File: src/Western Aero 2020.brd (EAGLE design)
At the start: 127.7 x 101.9 mm, 94 parts, among them IC1 LT1963AET, IC2 LT1963AET, J1 PITOT, J10 ANA_IO, J11 PWR, J12 POWER, J2 BUZZER, J3 RX2/TX2, J4 RX3/TX3, J5 SPI, J6 DIG_IO, J7 RX1/TX1, J8 DIG_IO, J9 REF/GND, U3 TEENSY_3.5_DIL+4, U5 SPARKFUN_MPU9250_IMU, U6 ADAFRUIT_MPL3115A2_BAROMETER, U7 ADAFRUIT_INA219_BATTERY_SENSOR, U8 ADAFRUIT_RFM95W_LORA_RADIO, U9 ADAFRUIT_MTK3339_GPS

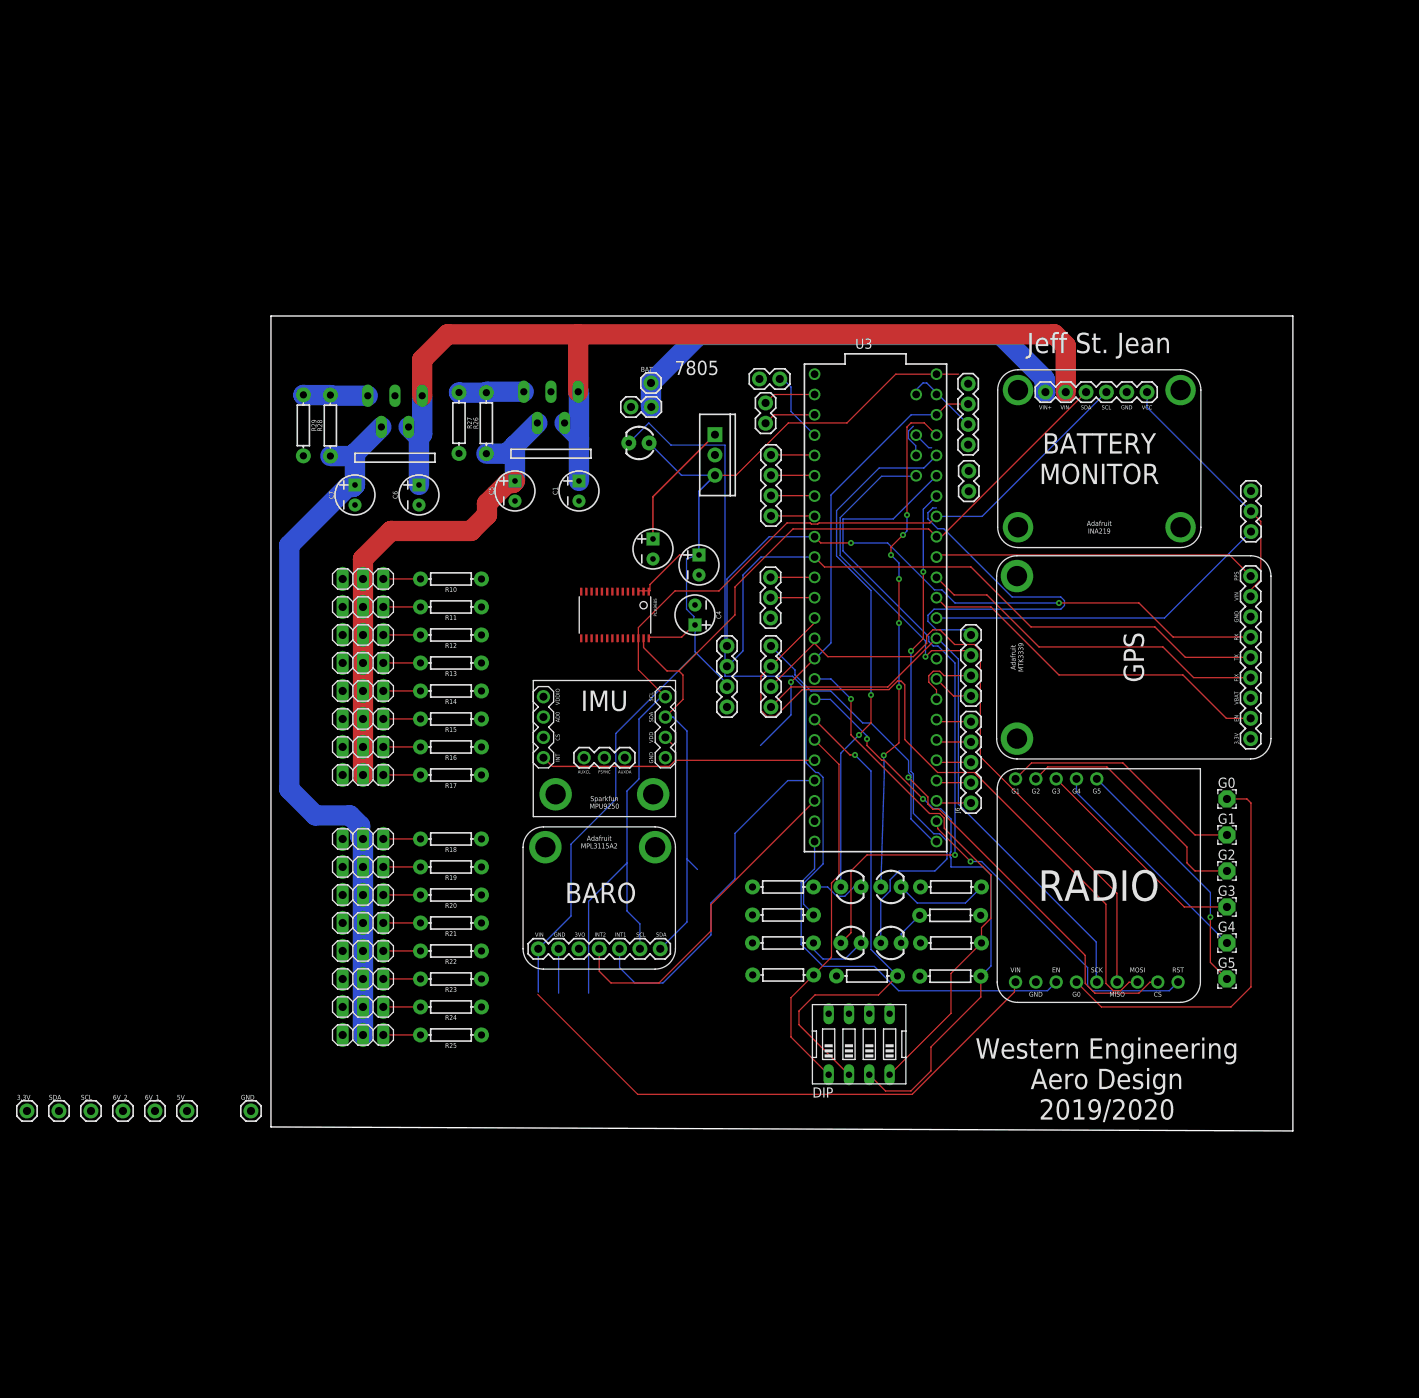
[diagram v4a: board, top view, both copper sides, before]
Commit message: Changed test point parts. Updated parts list. Adjusted board layout.
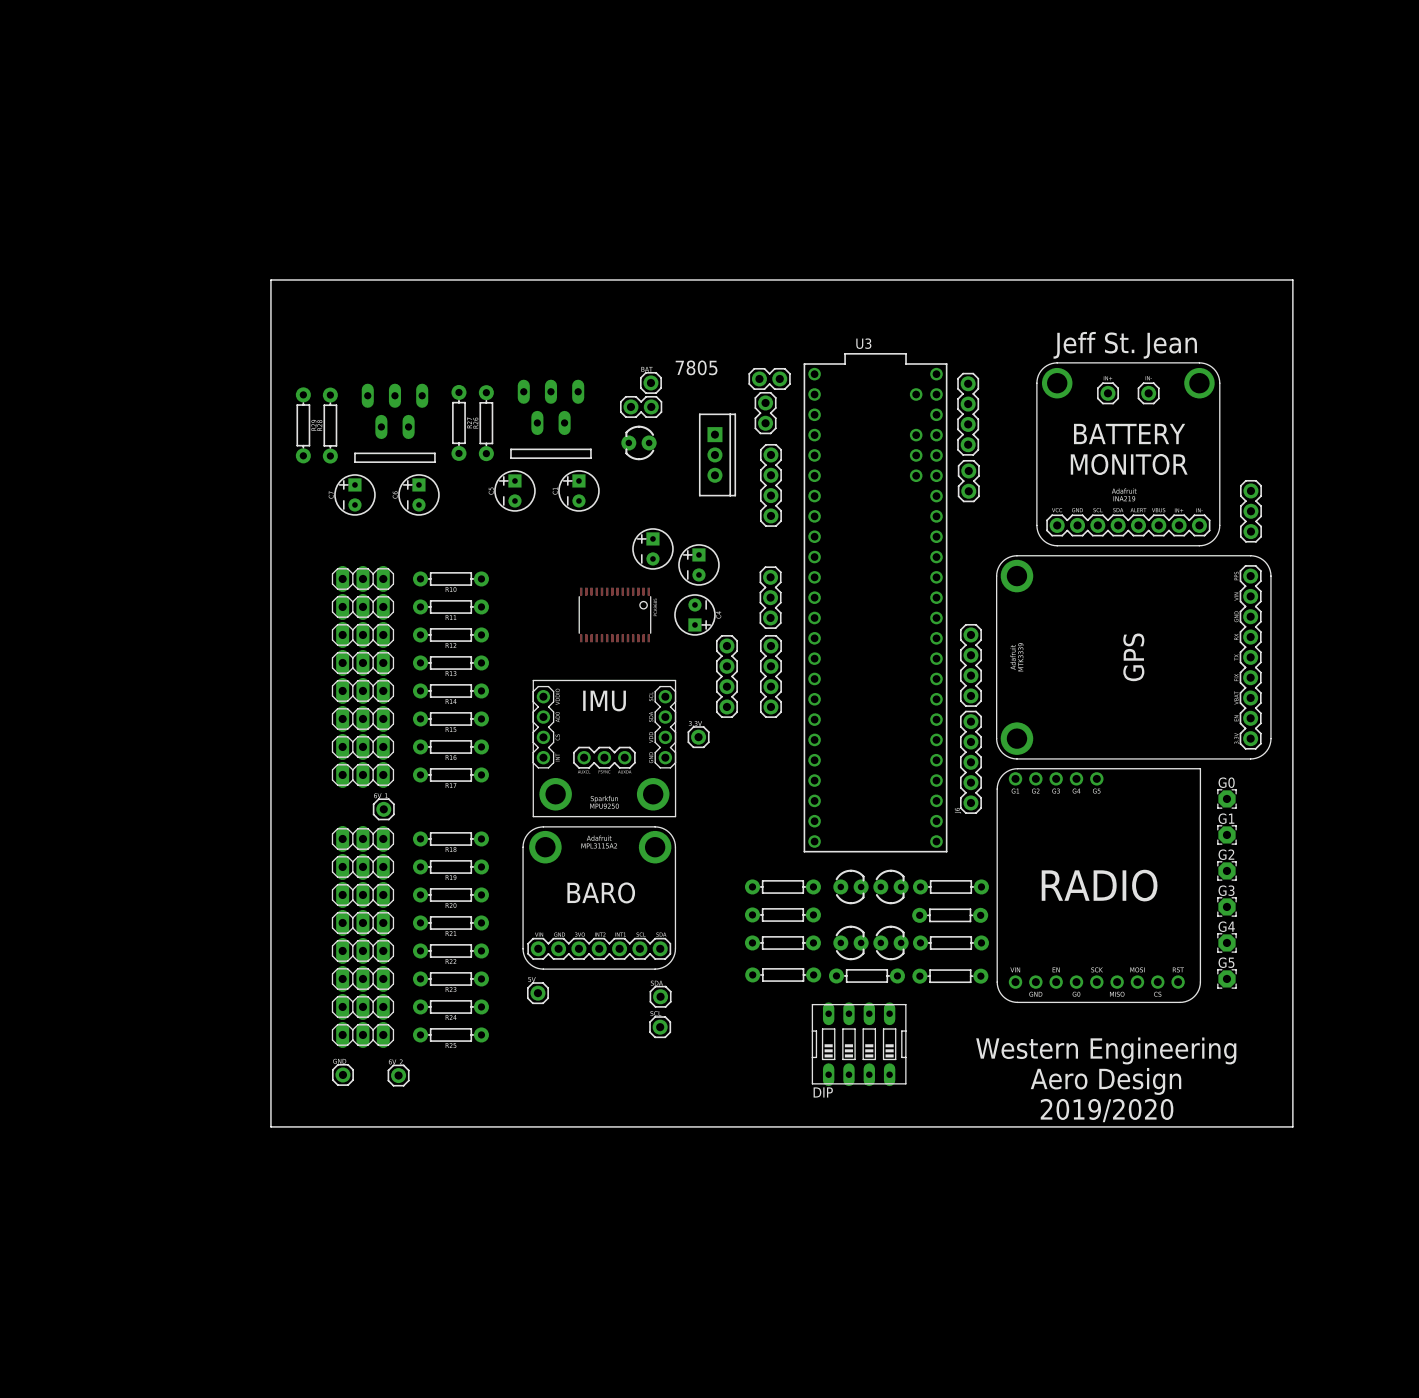
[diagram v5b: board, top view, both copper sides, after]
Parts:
- moved 3.3V 96.1 mm to (52.0, 49.2)
- moved SDA 76.5 mm to (47.2, 16.8)
- moved SCL 71.9 mm to (47.1, 13.0)
- moved 6V_1 47.3 mm to (12.6, 40.2)
- moved 5V 46.3 mm to (31.9, 17.2)
- moved 6V_2 34.7 mm to (14.4, 6.92)
- moved U7 30.1 mm to (94.2, 73.2), turned to 0 degrees
- moved GND 12.3 mm to (7.50, 7.00)
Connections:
- net D3: now also U7.ALERT
- net VIN+: now also U7.IN+_TER; no longer U7.VIN+
- net VIN-: now also U7.IN-_TER; no longer U7.VIN-
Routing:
- net 5V: track 246.6 -> 0.00 mm
- net VIN-: track 143.0 -> 0.00 mm
- net SCL: track 133.6 -> 0.00 mm
- net SDA: track 115.7 -> 0.00 mm
- net 6V_2: track 90.7 -> 0.00 mm
- net MOSI: track 89.8 -> 0.00 mm
- net BLUE_LED: track 85.4 -> 0.00 mm, vias 1 -> 0
- net N$6: track 84.7 -> 0.00 mm
- net TX3: track 81.9 -> 0.00 mm
- net MISO: track 81.8 -> 0.00 mm
- net RX3: track 81.2 -> 0.00 mm, vias 2 -> 0
- net CS: track 81.1 -> 0.00 mm, vias 1 -> 0
- net SCK: track 75.6 -> 0.00 mm
- net DIP2: track 72.6 -> 0.00 mm, vias 2 -> 0
- net DIP1: track 65.8 -> 0.00 mm, vias 1 -> 0
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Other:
- board size 127.7 x 101.9 mm -> 127.7 x 105.9 mm

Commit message: Finished new route.
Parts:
- removed J12: POWER, SparkFun-Connectors:1X02
- added BAT_GND, BAT_VIN: (no value), SparkFun-Connectors:1X01
- moved 5V 95.6 mm to (127.4, 13.2)
- moved U6 92.6 mm to (122.5, 23.7), turned to 180 degrees
- moved R4 82.6 mm to (32.5, 104.0), turned to 180 degrees
- moved 3.3V 78.9 mm to (128.4, 29.7)
- moved DIP 76.2 mm to (78.0, 86.8)
- moved J4 73.7 mm to (129.0, 58.5)
- moved J11 73.3 mm to (128.4, 33.9), turned to 90 degrees
- moved J7 67.8 mm to (123.1, 65.4), turned to 180 degrees
- moved U5 61.9 mm to (83.3, 22.8)
- moved G5 61.8 mm to (58.0, 4.00), turned to 270 degrees
- moved J2 60.1 mm to (115.0, 65.4), turned to 0 degrees
- moved U9 59.5 mm to (95.5, 99.0), turned to 270 degrees
- moved J1 59.2 mm to (87.0, 31.5), turned to 0 degrees
- moved G4 58.8 mm to (62.5, 4.00), turned to 270 degrees
- moved U7 58.1 mm to (46.7, 39.6), turned to 90 degrees
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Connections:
- net GND: now also BAT_GND.1; no longer J12.1
- net VIN+: now also BAT_VIN.1; no longer J12.2
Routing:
- net VIN-: track 0.00 -> 136.4 mm
- net SCL: track 0.00 -> 131.0 mm, vias 0 -> 1
- net SDA: track 0.00 -> 126.7 mm, vias 0 -> 1
- net 3.3V: track 0.00 -> 112.9 mm, vias 0 -> 1
- net D3: track 0.00 -> 77.1 mm, vias 0 -> 1
- net ENV_INT2: track 0.00 -> 65.4 mm, vias 0 -> 1
- net IMU_INT: track 0.00 -> 63.0 mm
- net PWM0: track 0.00 -> 62.1 mm
- net TX3: track 0.00 -> 61.0 mm
- net ENV_INT1: track 0.00 -> 60.7 mm
- net PWM15: track 0.00 -> 59.3 mm
- net PWM1: track 0.00 -> 58.3 mm
- net RX3: track 0.00 -> 57.3 mm
- net PWM14: track 0.00 -> 55.6 mm
- net PWM2: track 0.00 -> 54.6 mm
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- added copper zone on layer 1, net 5V
- added copper zone on layer 16, net GND
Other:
- board size 127.7 x 105.9 mm -> 133.7 x 108.9 mm
- board text removed: "7805"

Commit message: no message
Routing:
- net 5V: track 20.7 -> 16.4 mm
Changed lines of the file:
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@@
 <vertex x="29.5" y="107"/>
 </polygon>
-<wire x1="44.2" y1="42.19" x2="44.01" y2="42" width="0.2032" layer="1"/>
-<wire x1="44.01" y1="42" x2="40" y2="42" width="0.2032" layer="1"/>
 <wire x1="44.2" y1="42.19" x2="50.89" y2="35.5" width="0.2032" layer="16"/>
 <wire x1="50.89" y1="35.5" x2="51.5" y2="35.5" width="0.2032" layer="16"/>

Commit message: 14% reduction
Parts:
- moved D5 37.0 mm to (72.5, 85.5)
- moved R4 37.0 mm to (64.5, 85.5)
- moved C3 28.6 mm to (48.5, 66.2)
- moved PCA9685 26.6 mm to (36.5, 69.5)
- moved C2 20.0 mm to (48.2, 73.2)
- moved U9 18.7 mm to (78.0, 92.5)
- moved 7805 18.6 mm to (49.0, 83.5)
- moved 3.3V 18.5 mm to (111.0, 23.7)
- moved J11 18.3 mm to (110.9, 28.4)
- moved C4 17.8 mm to (39.0, 36.5)
- moved J9 17.7 mm to (111.5, 39.8)
- moved J4 17.6 mm to (111.5, 57.0)
- moved DIP 15.3 mm to (66.0, 77.3)
- moved 5V 15.1 mm to (112.4, 11.7)
- moved D1 15.1 mm to (93.0, 31.0)
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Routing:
- net PWM7: track 38.8 -> 11.2 mm
- net PWM2: track 54.6 -> 28.8 mm
- net PWM6: track 41.1 -> 15.3 mm
- net PWM5: track 43.3 -> 17.5 mm
- net PWM1: track 58.3 -> 32.6 mm
- net PWM0: track 62.1 -> 36.3 mm
- net PWM4: track 47.0 -> 21.3 mm
- net PWM3: track 50.8 -> 25.1 mm
- net VIN-: track 136.4 -> 119.3 mm
- net 5V: track 16.4 -> 0.00 mm, vias 1 -> 0
- net D3: track 77.1 -> 61.4 mm
- net DIP1: track 25.1 -> 15.9 mm
- net DIP3: track 26.1 -> 16.9 mm
- net DIP4: track 25.6 -> 16.4 mm
- net PWM11: track 44.3 -> 53.5 mm
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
